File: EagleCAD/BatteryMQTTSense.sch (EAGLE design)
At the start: 10 parts, among them CN1 1X4-BIG

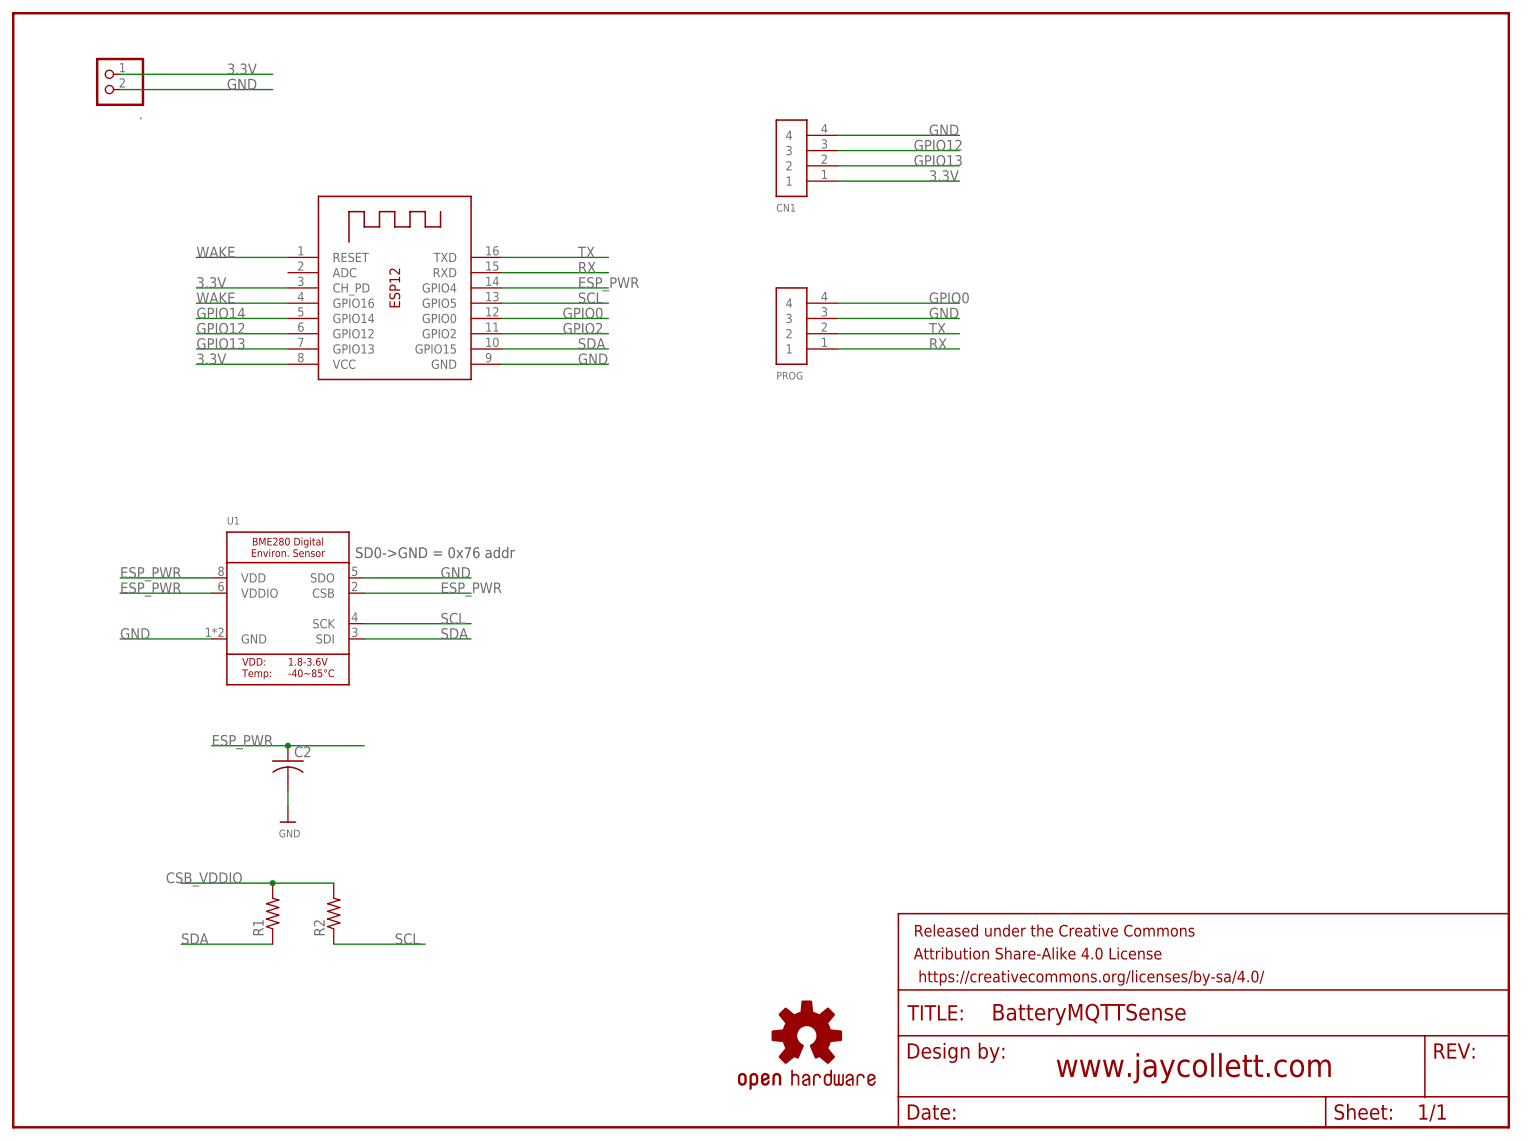
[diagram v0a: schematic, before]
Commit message: adding new design for eaglecad files, using daughterboard for bme
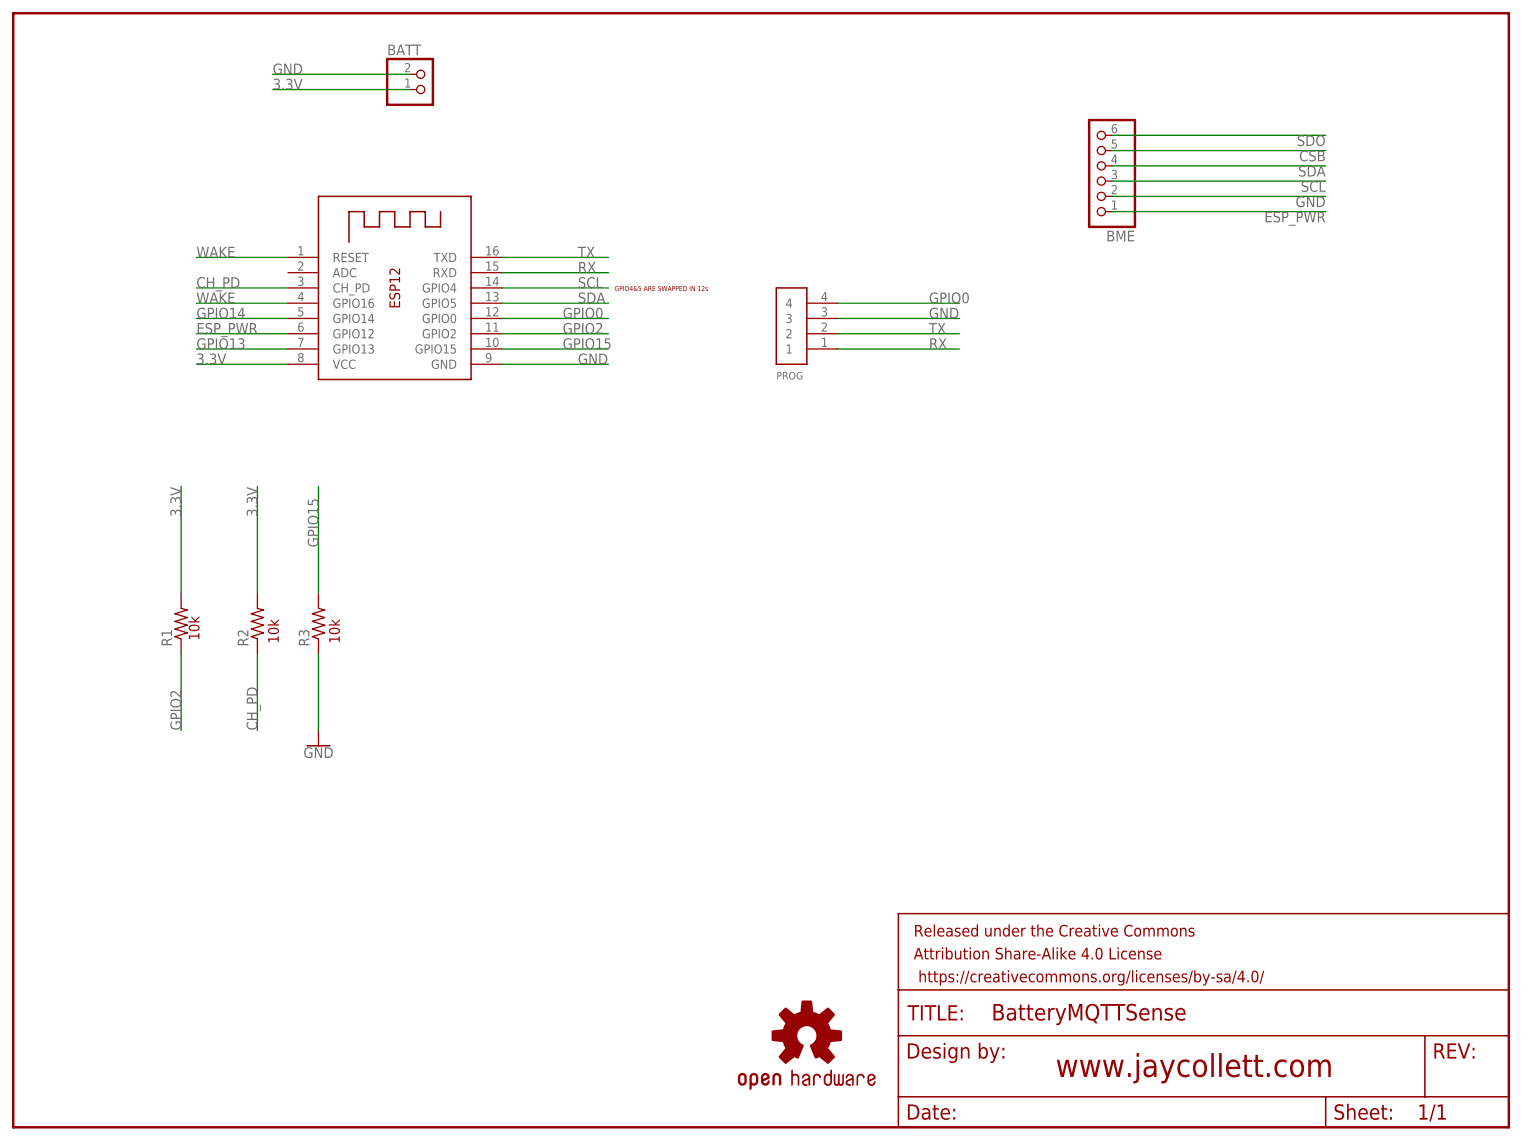
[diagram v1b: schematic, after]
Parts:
- removed .: (no value), adafruit:JST_2PIN-THM
- removed C2: (no value), adafruit:C-USC0805K
- removed CN1: 1X4-BIG, adafruit:1X4-BIG
- removed U1: (no value), Adafruit BME280:MICROBUILDER_BME280
- added BATT: (no value), adafruit:JST_2PIN-THM-RA
- added BME: (no value), adafruit:PINHD-1X6CB
- added R3: (no value), adafruit:R-US_M0805
- R1, R2: device adafruit:R-US_R0805 -> adafruit:R-US_M0805
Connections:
- removed net CSB_VDDIO: R1.2, R2.2
- removed net GPIO12: CN1.3, _.GPIO12
- new net CH_PD: R2.1, _.CH_PD
- new net CSB: BME.5
- new net GPIO15: R3.2, _.GPIO15
- new net SDO: BME.6
- net 3.3V: now also BATT.2, R1.2, R2.2; no longer ..2, CN1.1, _.CH_PD
- net ESP_PWR: now also BME.1, _.GPIO12; no longer C2.1, U1.CSB, U1.VDD, U1.VDDIO, _.GPIO4
- net GND: now also BATT.1, BME.2, R3.1; no longer ..1, C2.2, CN1.4, U1.GND, U1.SDO
- net GPIO13: no longer CN1.2
- net GPIO2: now also R1.1
- net SCL: now also BME.3, _.GPIO4; no longer R2.1, U1.SCK, _.GPIO5
- net SDA: now also BME.4, _.GPIO5; no longer R1.1, U1.SDI, _.GPIO15
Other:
- note added: "10k"
- note added: "GPIO4&5 ARE SWAPPED IN 12s"
- note removed: "SD0->GND = 0x76 addr"
- moved on the sheet: R1, R2

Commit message: updating schematic and board and added png file versions
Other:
- note added: "1.2"
- moved on the sheet: BATT, BME, PROG
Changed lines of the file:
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@@
 <text x="54.356" y="80.518" size="1.778" layer="94" rot="R90">10k</text>
 <text x="100.076" y="139.192" size="0.8128" layer="94">GPIO4&amp;5 ARE SWAPPED IN 12s</text>
+<text x="240.792" y="6.858" size="3.81" layer="94">1.2</text>
 </plain>
 <instances>
 <instance part="_" gate="G$1" x="63.5" y="139.7"/>
-<instance part="PROG" gate="G$1" x="132.08" y="132.08" rot="R180"/>
+<instance part="PROG" gate="G$1" x="83.82" y="76.2" rot="R180"/>
 <instance part="FRAME1" gate="G$1" x="0" y="0"/>
 <instance part="FRAME1" gate="V" x="147.32" y="0"/>
 <instance part="LOGO1" gate="G$1" x="132.08" y="15.24"/>
-<instance part="BATT" gate="G$1" x="68.58" y="172.72"/>
-<instance part="BME" gate="A" x="180.34" y="160.02" rot="R180"/>
+<instance part="BATT" gate="G$1" x="33.02" y="170.18"/>
+<instance part="BME" gate="A" x="78.74" y="101.6" rot="R180"/>
 <instance part="R1" gate="G$1" x="27.94" y="83.82" rot="R90"/>
 <instance part="R2" gate="G$1" x="40.64" y="83.82" rot="R90"/>
@@
 <segment>
 <pinref part="BATT" gate="G$1" pin="2"/>
-<wire x1="66.04" y1="172.72" x2="43.18" y2="172.72" width="0.1524" layer="91"/>
-<label x="43.18" y="172.72" size="1.778" layer="95"/>
+<wire x1="30.48" y1="170.18" x2="7.62" y2="170.18" width="0.1524" layer="91"/>
+<label x="7.62" y="170.18" size="1.778" layer="95"/>
 </segment>
 <segment>
@@
 <segment>
 <pinref part="PROG" gate="G$1" pin="3"/>
-<wire x1="137.16" y1="134.62" x2="157.48" y2="134.62" width="0.1524" layer="91"/>
-<label x="152.4" y="134.62" size="1.778" layer="95"/>
+<wire x1="88.9" y1="78.74" x2="109.22" y2="78.74" width="0.1524" layer="91"/>
+<label x="104.14" y="78.74" size="1.778" layer="95"/>
 </segment>
 <segment>
@@
 <segment>
 <pinref part="BATT" gate="G$1" pin="1"/>
-<wire x1="66.04" y1="175.26" x2="43.18" y2="175.26" width="0.1524" layer="91"/>
-<label x="43.18" y="175.26" size="1.778" layer="95"/>
+<wire x1="30.48" y1="172.72" x2="7.62" y2="172.72" width="0.1524" layer="91"/>
+<label x="7.62" y="172.72" size="1.778" layer="95"/>
 </segment>
 <segment>
 <pinref part="BME" gate="A" pin="2"/>
-<wire x1="182.88" y1="154.94" x2="218.44" y2="154.94" width="0.1524" layer="91"/>
-<label x="218.44" y="154.94" size="1.778" layer="95" rot="R180"/>
+<wire x1="81.28" y1="96.52" x2="116.84" y2="96.52" width="0.1524" layer="91"/>
+<label x="116.84" y="96.52" size="1.778" layer="95" rot="R180"/>
 </segment>
 <segment>
@@
 <segment>
 <pinref part="PROG" gate="G$1" pin="1"/>
-<wire x1="137.16" y1="129.54" x2="157.48" y2="129.54" width="0.1524" layer="91"/>
-<label x="152.4" y="129.54" size="1.778" layer="95"/>
+<wire x1="88.9" y1="73.66" x2="109.22" y2="73.66" width="0.1524" layer="91"/>
+<label x="104.14" y="73.66" size="1.778" layer="95"/>
 </segment>
 <segment>
@@
 <segment>
 <pinref part="PROG" gate="G$1" pin="2"/>
-<wire x1="137.16" y1="132.08" x2="157.48" y2="132.08" width="0.1524" layer="91"/>
-<label x="152.4" y="132.08" size="1.778" layer="95"/>
+<wire x1="88.9" y1="76.2" x2="109.22" y2="76.2" width="0.1524" layer="91"/>
+<label x="104.14" y="76.2" size="1.778" layer="95"/>
 </segment>
 <segment>
@@
 <segment>
 <pinref part="PROG" gate="G$1" pin="4"/>
-<wire x1="137.16" y1="137.16" x2="157.48" y2="137.16" width="0.1524" layer="91"/>
-<label x="152.4" y="137.16" size="1.778" layer="95"/>
+<wire x1="88.9" y1="81.28" x2="109.22" y2="81.28" width="0.1524" layer="91"/>
+<label x="104.14" y="81.28" size="1.778" layer="95"/>
 </segment>
 <segment>
@@
 <segment>
 <pinref part="BME" gate="A" pin="3"/>
-<wire x1="182.88" y1="157.48" x2="218.44" y2="157.48" width="0.1524" layer="91"/>
-<label x="218.44" y="157.48" size="1.778" layer="95" rot="R180"/>
+<wire x1="81.28" y1="99.06" x2="116.84" y2="99.06" width="0.1524" layer="91"/>
+<label x="116.84" y="99.06" size="1.778" layer="95" rot="R180"/>
 </segment>
 <segment>
@@
 <segment>
 <pinref part="BME" gate="A" pin="4"/>
-<wire x1="182.88" y1="160.02" x2="218.44" y2="160.02" width="0.1524" layer="91"/>
-<label x="218.44" y="160.02" size="1.778" layer="95" rot="R180"/>
+<wire x1="81.28" y1="101.6" x2="116.84" y2="101.6" width="0.1524" layer="91"/>
+<label x="116.84" y="101.6" size="1.778" layer="95" rot="R180"/>
 </segment>
 <segment>
@@
 <segment>
 <pinref part="BME" gate="A" pin="1"/>
-<wire x1="182.88" y1="152.4" x2="218.44" y2="152.4" width="0.1524" layer="91"/>
-<label x="218.44" y="152.4" size="1.778" layer="95" rot="R180"/>
+<wire x1="81.28" y1="93.98" x2="116.84" y2="93.98" width="0.1524" layer="91"/>
+<label x="116.84" y="93.98" size="1.778" layer="95" rot="R180"/>
 </segment>
 <segment>
@@
 <segment>
 <pinref part="BME" gate="A" pin="5"/>
-<wire x1="182.88" y1="162.56" x2="218.44" y2="162.56" width="0.1524" layer="91"/>
-<label x="218.44" y="162.56" size="1.778" layer="95" rot="R180"/>
+<wire x1="81.28" y1="104.14" x2="116.84" y2="104.14" width="0.1524" layer="91"/>
+<label x="116.84" y="104.14" size="1.778" layer="95" rot="R180"/>
 </segment>
 </net>
@@
 <segment>
 <pinref part="BME" gate="A" pin="6"/>
-<wire x1="182.88" y1="165.1" x2="218.44" y2="165.1" width="0.1524" layer="91"/>
-<label x="218.44" y="165.1" size="1.778" layer="95" rot="R180"/>
+<wire x1="81.28" y1="106.68" x2="116.84" y2="106.68" width="0.1524" layer="91"/>
+<label x="116.84" y="106.68" size="1.778" layer="95" rot="R180"/>
 </segment>
 </net>
